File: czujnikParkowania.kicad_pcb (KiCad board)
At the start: 2 copper layers, 43 parts, among them J1 Screw_Terminal_01x03, Q1 BC817, Q2 IRF7404, Q3 BC817, Q4 BC817, Q5 BC817, U1 DC56-11SEKWA, U2 LM7805_TO220, U3 HC-SR04, U4 ATmega328-AU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

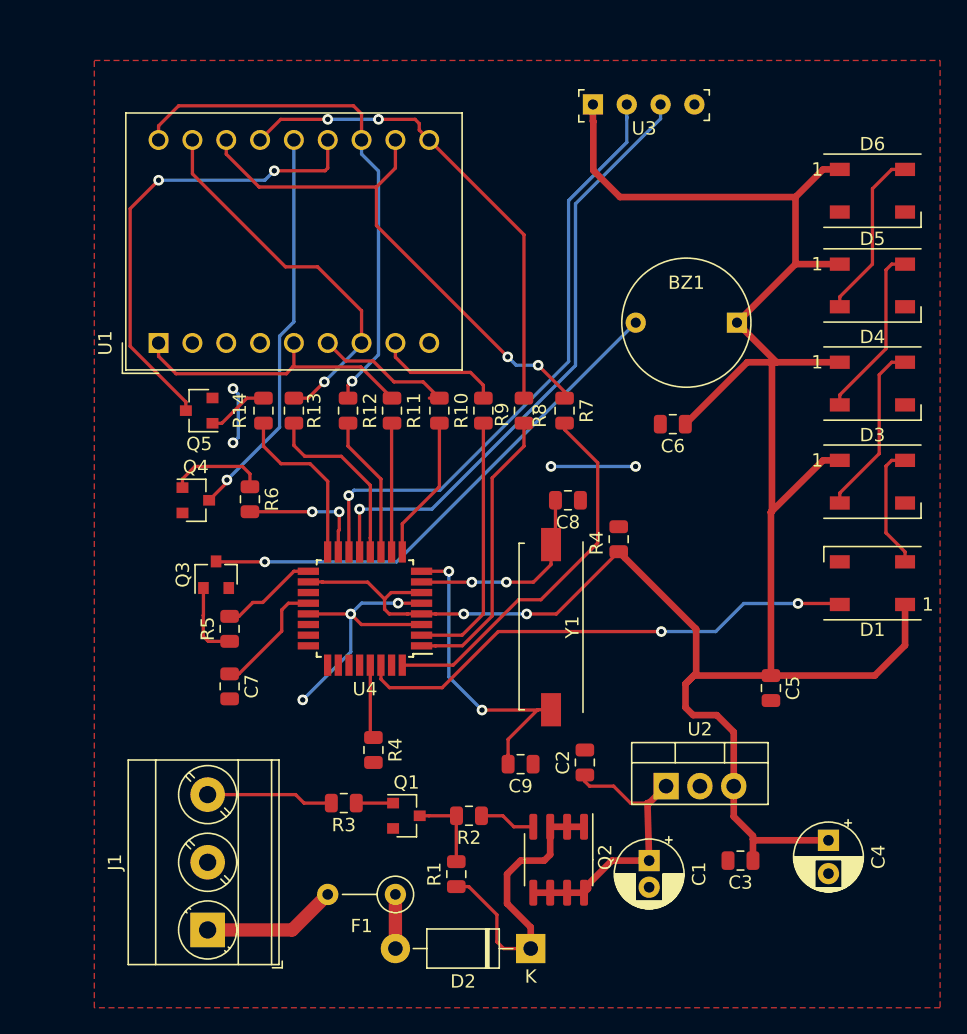
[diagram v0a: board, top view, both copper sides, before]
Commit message: Adruino and Atmega328 on single board for code dev
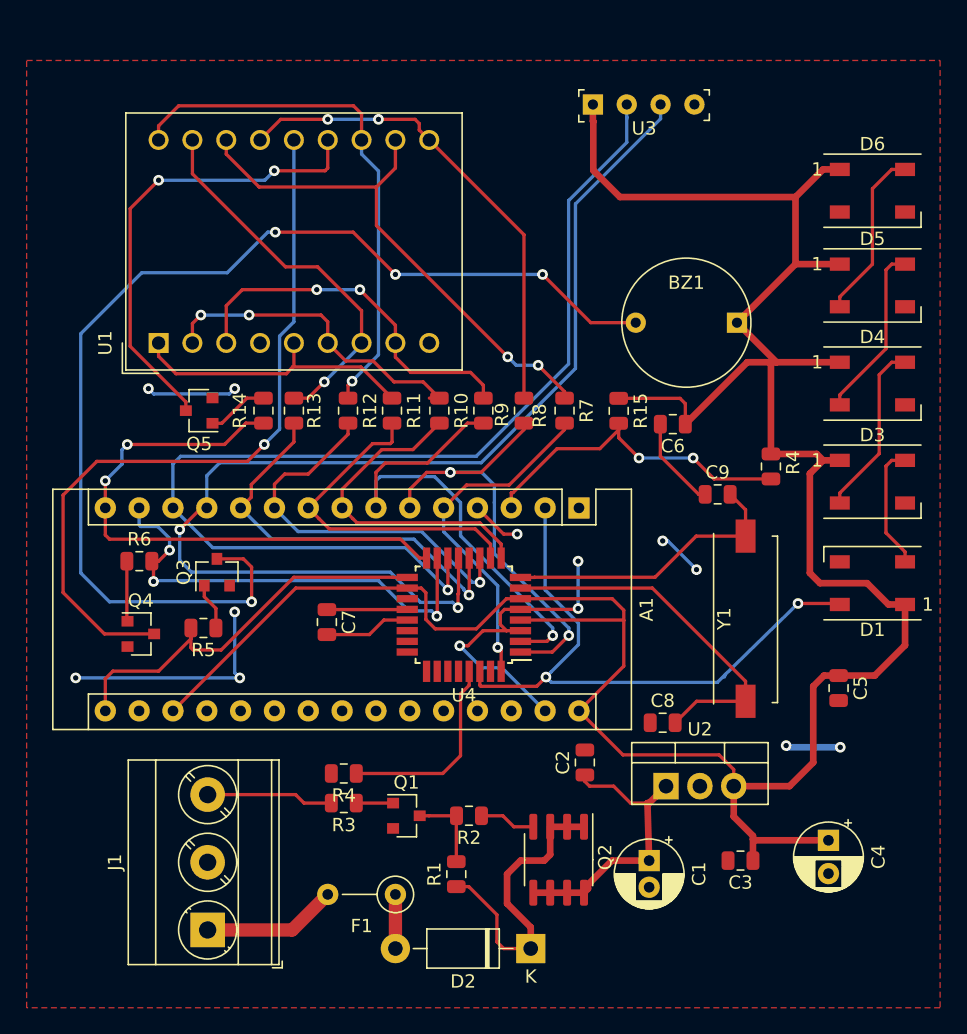
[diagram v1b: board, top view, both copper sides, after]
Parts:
- added A1: Arduino_Nano_v3.x, Module:Arduino_Nano, F.Cu at (56.7, 51.4)
- added R15: 1k, Resistor_SMD:R_0805_2012Metric, F.Cu at (59.7, 44.1)
- moved C9 25.1 mm to (67.1, 50.4), turned to 0 degrees
- moved C8 18.2 mm to (63.0, 67.5), turned to 0 degrees
- moved Y1 14.6 mm to (69.2, 59.7), turned to 270 degrees
- moved R4 12.7 mm to (71.1, 48.3), turned to 270 degrees
- moved Q4 10.8 mm to (23.8, 60.8)
- moved R6 9.52 mm to (23.7, 55.4), turned to 0 degrees
- moved C7 8.75 mm to (37.8, 59.9)
- moved U4 7.44 mm to (48.1, 59.4)
- moved C5 5.08 mm to (76.2, 64.9)
- moved R4 2.84 mm to (39.1, 71.3), turned to 180 degrees
- moved R5 1.97 mm to (28.5, 60.4), turned to 180 degrees
- moved Q3 0.20 mm to (29.5, 56.2)
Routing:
- net Net-(BZ1-Pad2): track 39.0 -> 84.8 mm, vias 1 -> 4
- net /ECHO: track 46.1 -> 87.0 mm, vias 1 -> 2
- net GND: track 33.2 -> 73.5 mm, vias 7 -> 13
- net /TRIG: track 46.2 -> 83.1 mm
- net /SEG_2: track 13.4 -> 43.2 mm, vias 0 -> 2
- net +5V: track 173.0 -> 201.8 mm, vias 2 -> 0
- net Net-(Q4-Pad3): track 30.2 -> 56.4 mm
- net Net-(A1-Pad28): track 0.00 -> 25.4 mm, vias 0 -> 2
- net /SEG_1: track 9.75 -> 34.9 mm, vias 2 -> 3
- net /BUZZER: track 7.31 -> 31.0 mm
- net /SEG_F: track 10.7 -> 29.3 mm, vias 0 -> 1
- net Net-(R9-Pad1): track 9.51 -> 27.9 mm, vias 0 -> 2
- net /SEG_C: track 19.7 -> 37.1 mm, vias 0 -> 1
- net /SEG_G: track 14.0 -> 31.0 mm, vias 0 -> 1
- net /SEG_E: track 9.68 -> 25.7 mm
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
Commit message: Added button
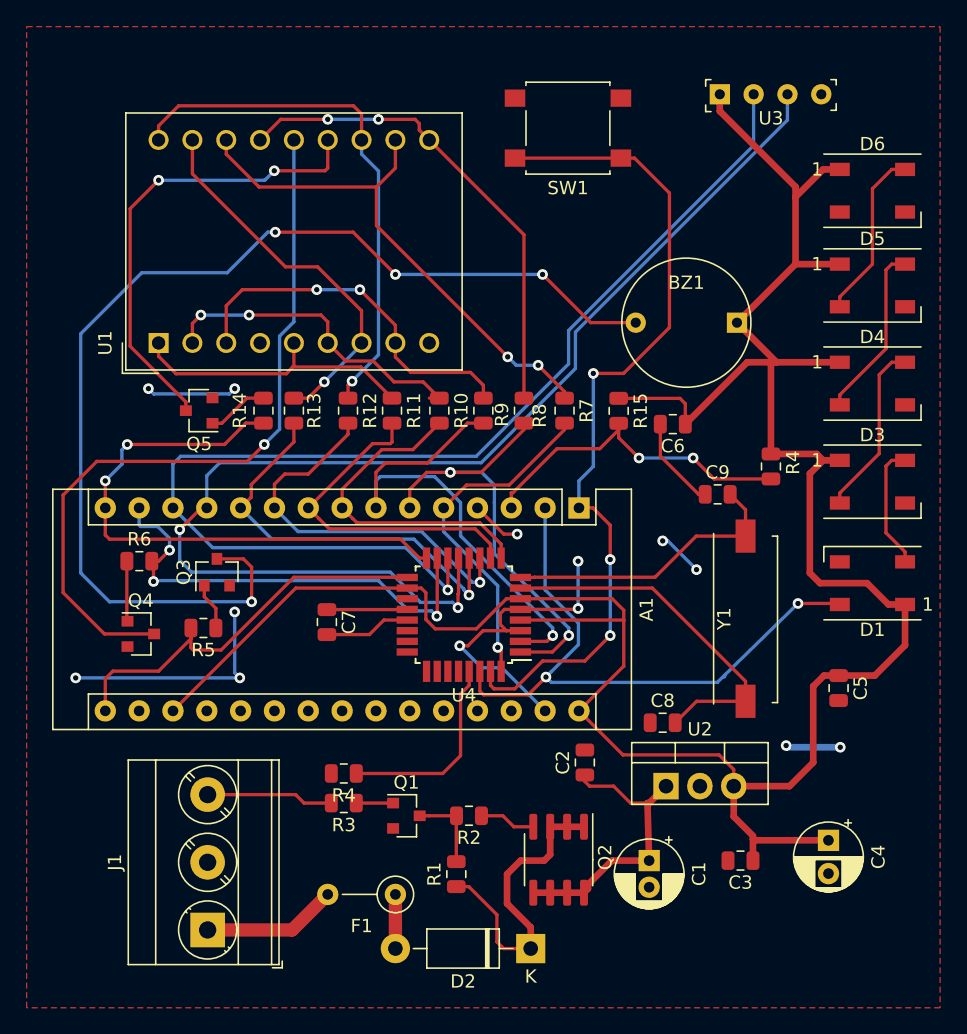
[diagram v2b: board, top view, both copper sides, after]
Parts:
- added SW1: SW_Push, Button_Switch_SMD:SW_SPST_B3S-1000, F.Cu at (55.9, 22.9)
- moved U3 9.56 mm to (71.1, 20.3)
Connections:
- A1 pad 1: Net-(A1-Pad1) -> /BTN
- U4 pad 31: /D1 -> /BTN
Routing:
- net /BTN: track 0.00 -> 63.4 mm, vias 0 -> 3
- net +5V: track 201.8 -> 190.9 mm
- net /ECHO: track 87.0 -> 91.7 mm
- net /TRIG: track 83.1 -> 87.7 mm
- net /RGB_DI: track 46.0 -> 46.8 mm

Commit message: bug on schematic and missing connection on PCB
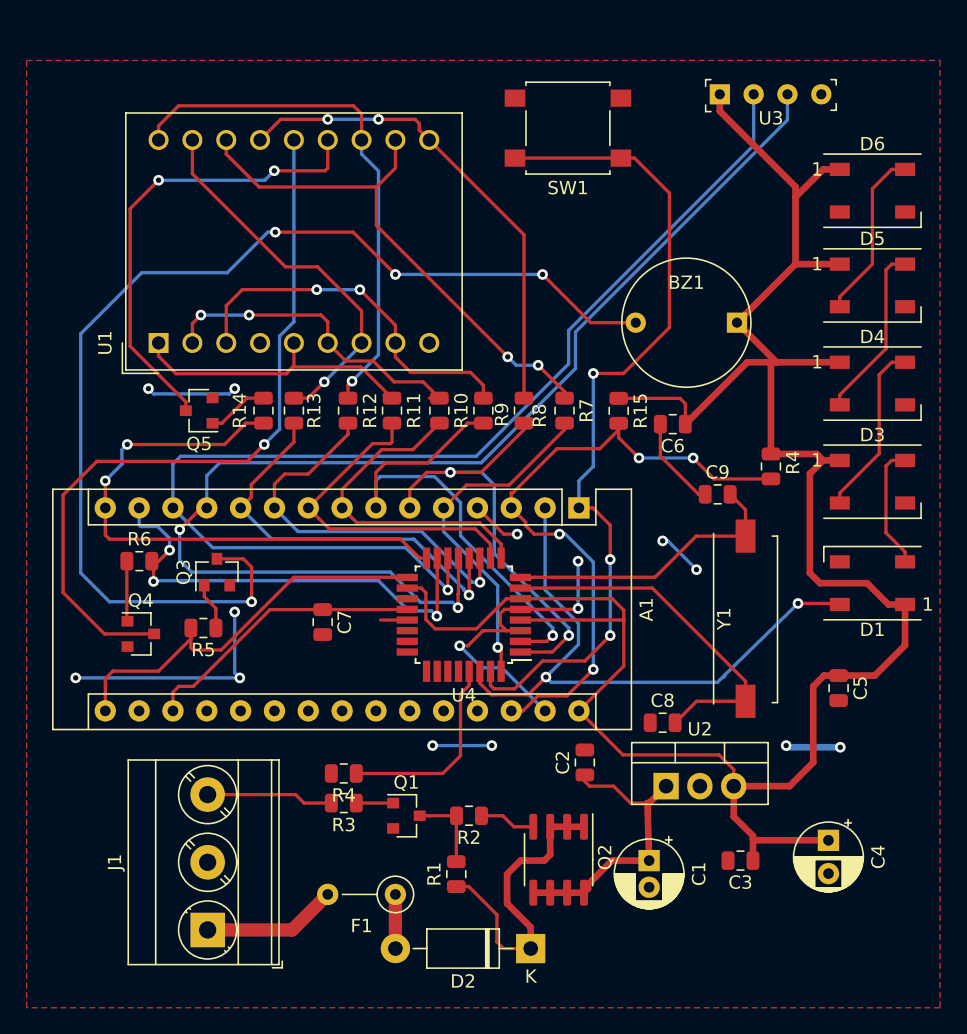
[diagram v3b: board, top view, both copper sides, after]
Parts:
- moved C7 0.32 mm to (37.5, 59.9)
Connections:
- A1 pad 18: +5V -> Net-(A1-Pad18)
- C7 pad 1: Net-(C7-Pad1) -> Net-(A1-Pad18)
- U4 pad 20: Net-(C7-Pad1) -> Net-(A1-Pad18)
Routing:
- net Net-(A1-Pad28): track 25.4 -> 48.9 mm, vias 2 -> 4
- net Net-(A1-Pad18): track 0.00 -> 21.8 mm
- net +5V: track 190.9 -> 169.5 mm
- net Net-(C7-Pad1): track 6.04 -> 0.00 mm
- net GND: vias 13 -> 15

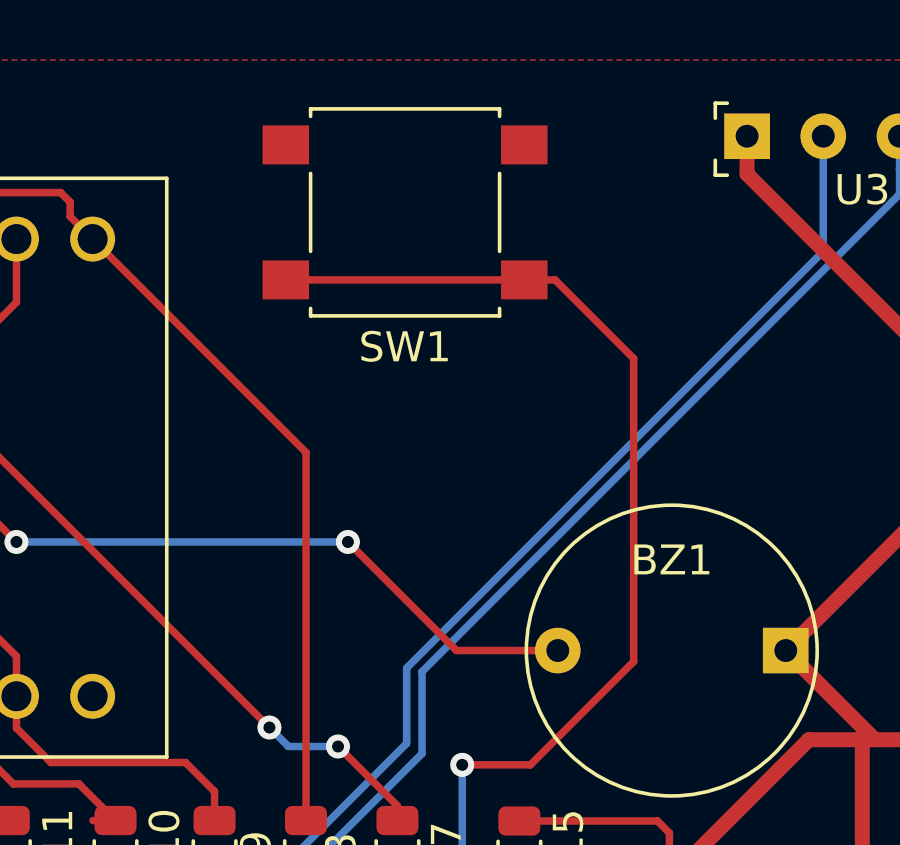
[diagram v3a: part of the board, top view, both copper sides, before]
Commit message: moved button
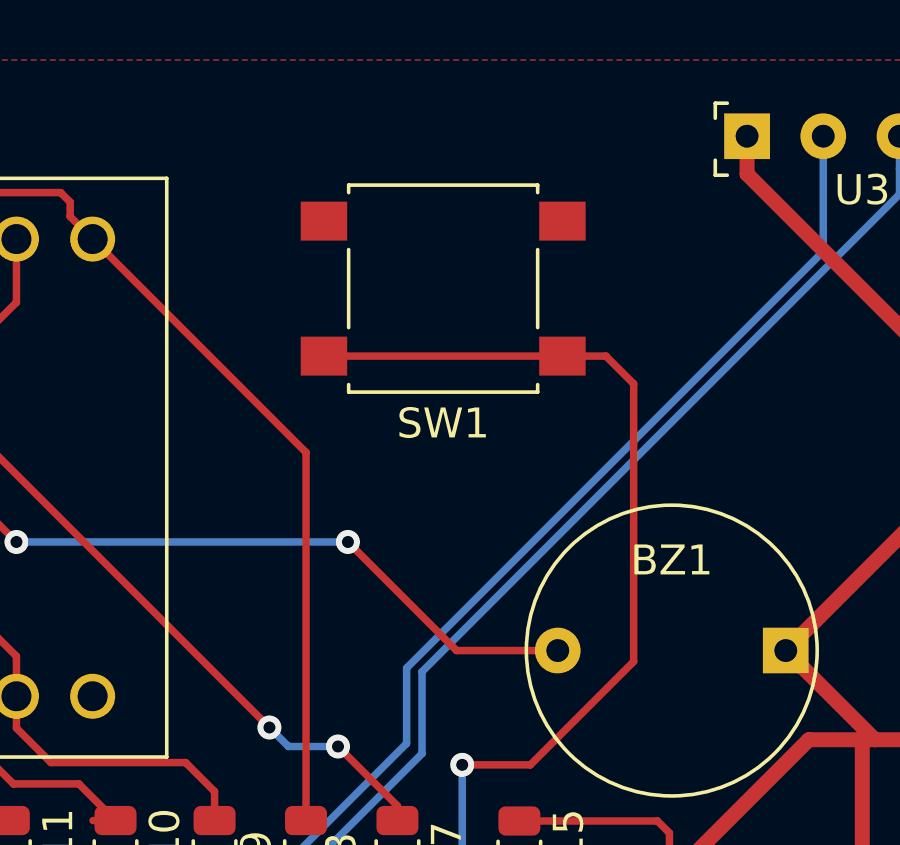
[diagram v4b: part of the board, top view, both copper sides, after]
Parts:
- moved SW1 2.84 mm to (57.1, 25.4)
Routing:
- net /BTN: track 63.4 -> 60.6 mm
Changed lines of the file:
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@@
   )
   (module Button_Switch_SMD:SW_SPST_B3S-1000 (layer F.Cu)
-    (at 55.88 22.86 180)
+    (at 57.15 25.4 180)
     (descr "Surface Mount Tactile Switch for High-Density Packaging")
     (tags "Tactile Switch")
@@
   (segment (start 36.068 73.533) (end 38.115 73.533) (width 0.25) (layer F.Cu) (net 44))
   (segment (start 35.433 72.898) (end 36.068 73.533) (width 0.25) (layer F.Cu) (net 44))
-  (segment (start 43.8 59.0065) (end 43.815 58.9915) (width 0.25) (layer F.Cu) (net 67))
-  (segment (start 37.7825 59.0065) (end 43.8 59.0065) (width 0.25) (layer F.Cu) (net 67))
   (segment (start 65.54 65.89) (end 63.9295 67.5005) (width 0.25) (layer F.Cu) (net 45))
   (segment (start 69.215 65.89) (end 65.54 65.89) (width 0.25) (layer F.Cu) (net 45))
@@
   (segment (start 46.482 71.3105) (end 39.99 71.3105) (width 0.25) (layer F.Cu) (net 47))
   (segment (start 47.8155 69.977) (end 46.482 71.3105) (width 0.25) (layer F.Cu) (net 47))
-  (segment (start 60.88 25.11) (end 63.5 27.73) (width 0.25) (layer F.Cu) (net 66))
-  (segment (start 59.855 25.11) (end 60.88 25.11) (width 0.25) (layer F.Cu) (net 66))
   (via (at 57.785 41.275) (size 0.8) (drill 0.4) (layers F.Cu B.Cu) (net 66))
   (segment (start 60.05715 41.275) (end 57.785 41.275) (width 0.25) (layer F.Cu) (net 66))
-  (segment (start 63.5 27.73) (end 63.5 37.83215) (width 0.25) (layer F.Cu) (net 66))
   (segment (start 63.5 37.83215) (end 60.05715 41.275) (width 0.25) (layer F.Cu) (net 66))
   (segment (start 57.785 41.275) (end 57.785 48.26) (width 0.25) (layer B.Cu) (net 66))
@@
   (segment (start 59.055 52.671) (end 57.7555 51.3715) (width 0.25) (layer F.Cu) (net 66))
   (segment (start 59.055 55.245) (end 59.055 52.671) (width 0.25) (layer F.Cu) (net 66))
-  (segment (start 59.855 25.11) (end 51.905 25.11) (width 0.25) (layer F.Cu) (net 66))
+  (segment (start 61.125 27.65) (end 62.575 27.65) (width 0.25) (layer F.Cu) (net 66))
+  (segment (start 63.5 28.575) (end 63.5 37.83215) (width 0.25) (layer F.Cu) (net 66))
+  (segment (start 62.575 27.65) (end 63.5 28.575) (width 0.25) (layer F.Cu) (net 66))
+  (segment (start 61.125 27.65) (end 53.175 27.65) (width 0.25) (layer F.Cu) (net 66))
+  (segment (start 43.8 59.0065) (end 43.815 58.9915) (width 0.25) (layer F.Cu) (net 67))
+  (segment (start 37.7825 59.0065) (end 43.8 59.0065) (width 0.25) (layer F.Cu) (net 67))
   (segment (start 26.411901 67.061509) (end 26.2255 67.061509) (width 0.25) (layer F.Cu) (net 67))
   (segment (start 33.51441 59.0065) (end 27.75091 64.77) (width 0.25) (layer F.Cu) (net 67))
